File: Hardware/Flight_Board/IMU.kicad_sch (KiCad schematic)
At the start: 1 part

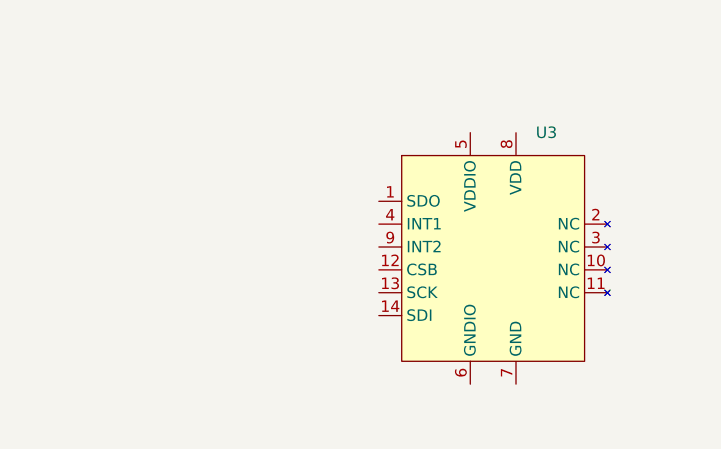
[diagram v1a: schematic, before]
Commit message: standardize connections and create initial spi2 bus
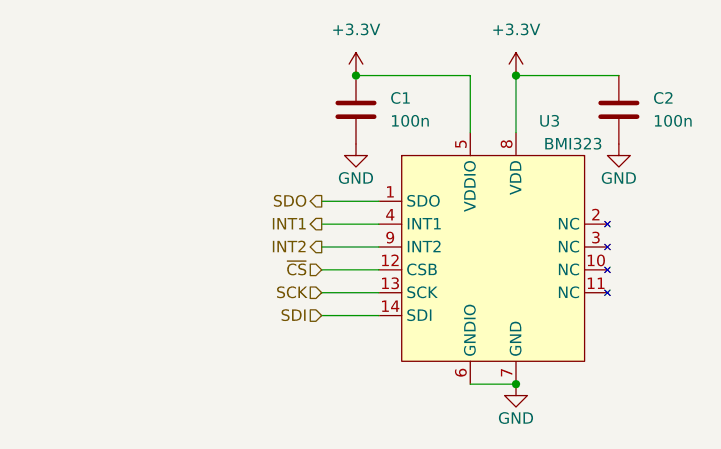
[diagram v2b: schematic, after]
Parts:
- added C1, C2: 100n, symbol Device:C
- U3: value ~ -> BMI323
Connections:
- net SDO: now reaches U3.1 (SDO)
- net ~{CS}: now reaches U3.12 (CSB)
- net SCK: now reaches U3.13 (SCK)
- net SDI: now reaches U3.14 (SDI)
- net INT1: now reaches U3.4 (INT1)
- net +3.3V: now reaches U3.5 (VDDIO)
- net +3.3V: now also U3.8 (VDD), C1.1, C2.1
- net GND: now reaches U3.6 (GNDIO)
- net GND: now also U3.7 (GND), C1.2, C2.2
- net INT2: now reaches U3.9 (INT2)

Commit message: clean up and finalize initial design
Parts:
- renumbered C1 to C?, C2 to C?, U3 to U6
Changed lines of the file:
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@@
   (symbol (lib_id "Device:C") (at 168.91 69.85 0) (unit 1)
     (in_bom yes) (on_board yes) (dnp no) (fields_autoplaced)
-    (property "Reference" "C1" (at 172.72 68.58 0)
+    (property "Reference" "C?" (at 172.72 68.58 0)
       (effects (font (size 1.27 1.27)) (justify left))
     )
@@
       (project "Flight_Board"
         (path "/e8eb85d5-f1ff-4500-895d-25b9ff5f6d36/438715e3-b069-4320-9581-dc19d9c2cf0e"
-          (reference "C1") (unit 1)
-        )
-        (path "/e8eb85d5-f1ff-4500-895d-25b9ff5f6d36/676308d2-6f42-4cc0-804f-a459182d1a62"
-          (reference "C15") (unit 1)
+          (reference "C?") (unit 1)
+        )
+        (path "/e8eb85d5-f1ff-4500-895d-25b9ff5f6d36/676308d2-6f42-4cc0-804f-a459182d1a62"
+          (reference "C18") (unit 1)
         )
       )
@@
   (symbol (lib_id "power:GND") (at 168.91 73.66 0) (unit 1)
     (in_bom yes) (on_board yes) (dnp no)
-    (property "Reference" "#PWR024" (at 168.91 80.01 0)
+    (property "Reference" "#PWR?" (at 168.91 80.01 0)
       (effects (font (size 1.27 1.27)) hide)
     )
@@
       (project "Flight_Board"
         (path "/e8eb85d5-f1ff-4500-895d-25b9ff5f6d36/438715e3-b069-4320-9581-dc19d9c2cf0e"
-          (reference "#PWR024") (unit 1)
-        )
-        (path "/e8eb85d5-f1ff-4500-895d-25b9ff5f6d36/676308d2-6f42-4cc0-804f-a459182d1a62"
-          (reference "#PWR027") (unit 1)
+          (reference "#PWR?") (unit 1)
+        )
+        (path "/e8eb85d5-f1ff-4500-895d-25b9ff5f6d36/676308d2-6f42-4cc0-804f-a459182d1a62"
+          (reference "#PWR035") (unit 1)
         )
       )
@@
   (symbol (lib_id "power:GND") (at 186.69 100.33 0) (unit 1)
     (in_bom yes) (on_board yes) (dnp no)
-    (property "Reference" "#PWR016" (at 186.69 106.68 0)
+    (property "Reference" "#PWR?" (at 186.69 106.68 0)
       (effects (font (size 1.27 1.27)) hide)
     )
@@
       (project "Flight_Board"
         (path "/e8eb85d5-f1ff-4500-895d-25b9ff5f6d36/438715e3-b069-4320-9581-dc19d9c2cf0e"
-          (reference "#PWR016") (unit 1)
-        )
-        (path "/e8eb85d5-f1ff-4500-895d-25b9ff5f6d36/676308d2-6f42-4cc0-804f-a459182d1a62"
-          (reference "#PWR029") (unit 1)
+          (reference "#PWR?") (unit 1)
+        )
+        (path "/e8eb85d5-f1ff-4500-895d-25b9ff5f6d36/676308d2-6f42-4cc0-804f-a459182d1a62"
+          (reference "#PWR037") (unit 1)
         )
       )
@@
   (symbol (lib_id "power:+3.3V") (at 168.91 66.04 0) (unit 1)
     (in_bom yes) (on_board yes) (dnp no) (fields_autoplaced)
-    (property "Reference" "#PWR025" (at 168.91 69.85 0)
+    (property "Reference" "#PWR?" (at 168.91 69.85 0)
       (effects (font (size 1.27 1.27)) hide)
     )
@@
       (project "Flight_Board"
         (path "/e8eb85d5-f1ff-4500-895d-25b9ff5f6d36/438715e3-b069-4320-9581-dc19d9c2cf0e"
-          (reference "#PWR025") (unit 1)
-        )
-        (path "/e8eb85d5-f1ff-4500-895d-25b9ff5f6d36/676308d2-6f42-4cc0-804f-a459182d1a62"
-          (reference "#PWR026") (unit 1)
+          (reference "#PWR?") (unit 1)
+        )
+        (path "/e8eb85d5-f1ff-4500-895d-25b9ff5f6d36/676308d2-6f42-4cc0-804f-a459182d1a62"
+          (reference "#PWR034") (unit 1)
         )
       )
@@
   (symbol (lib_id "Device:C") (at 198.12 69.85 0) (unit 1)
     (in_bom yes) (on_board yes) (dnp no) (fields_autoplaced)
-    (property "Reference" "C2" (at 201.93 68.58 0)
+    (property "Reference" "C?" (at 201.93 68.58 0)
       (effects (font (size 1.27 1.27)) (justify left))
     )
@@
       (project "Flight_Board"
         (path "/e8eb85d5-f1ff-4500-895d-25b9ff5f6d36/438715e3-b069-4320-9581-dc19d9c2cf0e"
-          (reference "C2") (unit 1)
-        )
-        (path "/e8eb85d5-f1ff-4500-895d-25b9ff5f6d36/676308d2-6f42-4cc0-804f-a459182d1a62"
-          (reference "C16") (unit 1)
+          (reference "C?") (unit 1)
+        )
+        (path "/e8eb85d5-f1ff-4500-895d-25b9ff5f6d36/676308d2-6f42-4cc0-804f-a459182d1a62"
+          (reference "C19") (unit 1)
         )
       )
@@
   (symbol (lib_id "Project:BMI323") (at 184.15 86.36 0) (unit 1)
     (in_bom yes) (on_board yes) (dnp no)
-    (property "Reference" "U3" (at 189.23 71.12 0)
+    (property "Reference" "U6" (at 189.23 71.12 0)
       (effects (font (size 1.27 1.27)) (justify left))
     )
@@
       (project "Flight_Board"
         (path "/e8eb85d5-f1ff-4500-895d-25b9ff5f6d36/676308d2-6f42-4cc0-804f-a459182d1a62"
-          (reference "U3") (unit 1)
+          (reference "U6") (unit 1)
         )
       )
@@
   (symbol (lib_id "power:+3.3V") (at 186.69 66.04 0) (unit 1)
     (in_bom yes) (on_board yes) (dnp no) (fields_autoplaced)
-    (property "Reference" "#PWR023" (at 186.69 69.85 0)
+    (property "Reference" "#PWR?" (at 186.69 69.85 0)
       (effects (font (size 1.27 1.27)) hide)
     )
@@
       (project "Flight_Board"
         (path "/e8eb85d5-f1ff-4500-895d-25b9ff5f6d36/438715e3-b069-4320-9581-dc19d9c2cf0e"
-          (reference "#PWR023") (unit 1)
-        )
-        (path "/e8eb85d5-f1ff-4500-895d-25b9ff5f6d36/676308d2-6f42-4cc0-804f-a459182d1a62"
-          (reference "#PWR028") (unit 1)
+          (reference "#PWR?") (unit 1)
+        )
+        (path "/e8eb85d5-f1ff-4500-895d-25b9ff5f6d36/676308d2-6f42-4cc0-804f-a459182d1a62"
+          (reference "#PWR036") (unit 1)
         )
       )
@@
   (symbol (lib_id "power:GND") (at 198.12 73.66 0) (unit 1)
     (in_bom yes) (on_board yes) (dnp no)
-    (property "Reference" "#PWR022" (at 198.12 80.01 0)
+    (property "Reference" "#PWR?" (at 198.12 80.01 0)
       (effects (font (size 1.27 1.27)) hide)
     )
@@
       (project "Flight_Board"
         (path "/e8eb85d5-f1ff-4500-895d-25b9ff5f6d36/438715e3-b069-4320-9581-dc19d9c2cf0e"
-          (reference "#PWR022") (unit 1)
-        )
-        (path "/e8eb85d5-f1ff-4500-895d-25b9ff5f6d36/676308d2-6f42-4cc0-804f-a459182d1a62"
-          (reference "#PWR030") (unit 1)
-        )
-      )
+          (reference "#PWR?") (unit 1)
+        )
+        (path "/e8eb85d5-f1ff-4500-895d-25b9ff5f6d36/676308d2-6f42-4cc0-804f-a459182d1a62"
+          (reference "#PWR038") (unit 1)
+        )
+      )

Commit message: clean up, implement suggestions from saunders
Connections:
- net INT2: no longer names the net of U6.9 (INT2)
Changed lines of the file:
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@@
-    (stroke (width 0) (type default))
-  )
-  (wire (pts (xy 165.1 85.09) (xy 171.45 85.09))
     (stroke (width 0) (type default))
   )
@@
     (effects (font (size 1.27 1.27)) (justify right))
   )
-  (hierarchical_label "INT2" (shape output) (at 165.1 85.09 180) (fields_autoplaced)
-    (effects (font (size 1.27 1.27)) (justify right))
-  )

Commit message: Add LEDs and test points
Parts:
- added TP2: IMU_INT, symbol Connector:TestPoint
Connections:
- net INT1: now also TP2.1
- net SDI renamed MOSI
- net SDO renamed MISO
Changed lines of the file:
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@@
   (junction (at 186.69 100.33) (diameter 0) (color 0 0 0 0)
+  )
+  (junction (at 144.78 82.55) (diameter 0) (color 0 0 0 0)
   )
   (junction (at 168.91 66.04) (diameter 0) (color 0 0 0 0)
@@
     (stroke (width 0) (type default))
   )
+  (wire (pts (xy 144.78 82.55) (xy 171.45 82.55))
+    (stroke (width 0) (type default))
+  )
   (wire (pts (xy 165.1 80.01) (xy 171.45 80.01))
     (stroke (width 0) (type default))
   )
   (wire (pts (xy 165.1 90.17) (xy 171.45 90.17))
+    (stroke (width 0) (type default))
+  )
+  (wire (pts (xy 144.78 77.47) (xy 144.78 82.55))
     (stroke (width 0) (type default))
   )
@@
     (stroke (width 0) (type default))
   )
-  (wire (pts (xy 165.1 82.55) (xy 171.45 82.55))
+  (wire (pts (xy 138.43 82.55) (xy 144.78 82.55))
     (stroke (width 0) (type default))
   )
@@
     (stroke (width 0) (type default))
   )
-  (hierarchical_label "SDO" (shape output) (at 165.1 80.01 180) (fields_autoplaced)
+  (hierarchical_label "MISO" (shape output) (at 165.1 80.01 180) (fields_autoplaced)
     (effects (font (size 1.27 1.27)) (justify right))
   )
@@
     (effects (font (size 1.27 1.27)) (justify right))
   )
-  (hierarchical_label "SDI" (shape input) (at 165.1 92.71 180) (fields_autoplaced)
+  (hierarchical_label "MOSI" (shape input) (at 165.1 92.71 180) (fields_autoplaced)
     (effects (font (size 1.27 1.27)) (justify right))
   )
-  (hierarchical_label "INT1" (shape output) (at 165.1 82.55 180) (fields_autoplaced)
+  (hierarchical_label "INT1" (shape output) (at 138.43 82.55 180) (fields_autoplaced)
     (effects (font (size 1.27 1.27)) (justify right))
   )
@@
         )
       )
+    )
+  )
+  (symbol (lib_id "Connector:TestPoint") (at 144.78 77.47 0) (unit 1)
+    (in_bom yes) (on_board yes) (dnp no)
+    (property "Reference" "TP2" (at 149.86 74.168 90)
+      (effects (font (size 1.27 1.27)) hide)
+    )
+    (property "Value" "IMU_INT" (at 143.51 72.39 0)
+      (effects (font (size 1.27 1.27)) (justify left))
+    )
+    (property "Footprint" "" (at 149.86 77.47 0)
+      (effects (font (size 1.27 1.27)) hide)
+    )
+    (property "Datasheet" "~" (at 149.86 77.47 0)
+      (effects (font (size 1.27 1.27)) hide)
+    )
+    (pin "1")
+    (instances
+      (project "Flight_Board"
+        (path "/e8eb85d5-f1ff-4500-895d-25b9ff5f6d36/bc23ea56-d50e-4ce7-856f-e38dfbe72971"
+          (reference "TP2") (unit 1)
+        )
+        (path "/e8eb85d5-f1ff-4500-895d-25b9ff5f6d36/43c0adf1-436b-4b66-9010-44cf9a79cc96"
+          (reference "TP3") (unit 1)
+        )
+        (path "/e8eb85d5-f1ff-4500-895d-25b9ff5f6d36/7c06db2a-34f5-45c0-9668-fbbbd940678c"
+          (reference "TP11") (unit 1)
+        )
+        (path "/e8eb85d5-f1ff-4500-895d-25b9ff5f6d36/52cae81a-54fe-42c0-9a19-be88b271d004"
+          (reference "TP14") (unit 1)
+        )
+        (path "/e8eb85d5-f1ff-4500-895d-25b9ff5f6d36/676308d2-6f42-4cc0-804f-a459182d1a62"
+          (reference "TP16") (unit 1)
+        )
+      )

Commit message: final touches, bom, footprints
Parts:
- C? (x2): footprint (none) -> Capacitor_SMD:C_0603_1608Metric_Pad1.08x0.95mm_HandSolder
- TP2: footprint (none) -> TestPoint:TestPoint_THTPad_2.0x2.0mm_Drill1.0mm
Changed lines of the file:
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@@
       (effects (font (size 1.27 1.27)) (justify left))
     )
-    (property "Footprint" "" (at 169.8752 73.66 0)
+    (property "Footprint" "Capacitor_SMD:C_0603_1608Metric_Pad1.08x0.95mm_HandSolder" (at 169.8752 73.66 0)
       (effects (font (size 1.27 1.27)) hide)
     )
@@
       (effects (font (size 1.27 1.27)) (justify left))
     )
-    (property "Footprint" "" (at 149.86 77.47 0)
+    (property "Footprint" "TestPoint:TestPoint_THTPad_2.0x2.0mm_Drill1.0mm" (at 149.86 77.47 0)
       (effects (font (size 1.27 1.27)) hide)
     )
@@
       (effects (font (size 1.27 1.27)) (justify left))
     )
-    (property "Footprint" "" (at 199.0852 73.66 0)
+    (property "Footprint" "Capacitor_SMD:C_0603_1608Metric_Pad1.08x0.95mm_HandSolder" (at 199.0852 73.66 0)
       (effects (font (size 1.27 1.27)) hide)
     )
